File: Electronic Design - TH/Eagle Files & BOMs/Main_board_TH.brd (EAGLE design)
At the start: 90 x 130 mm, 39 parts, among them M1 ARDUINO-NANO-3.0, Q1 IRF9520, Q2 IRF9520

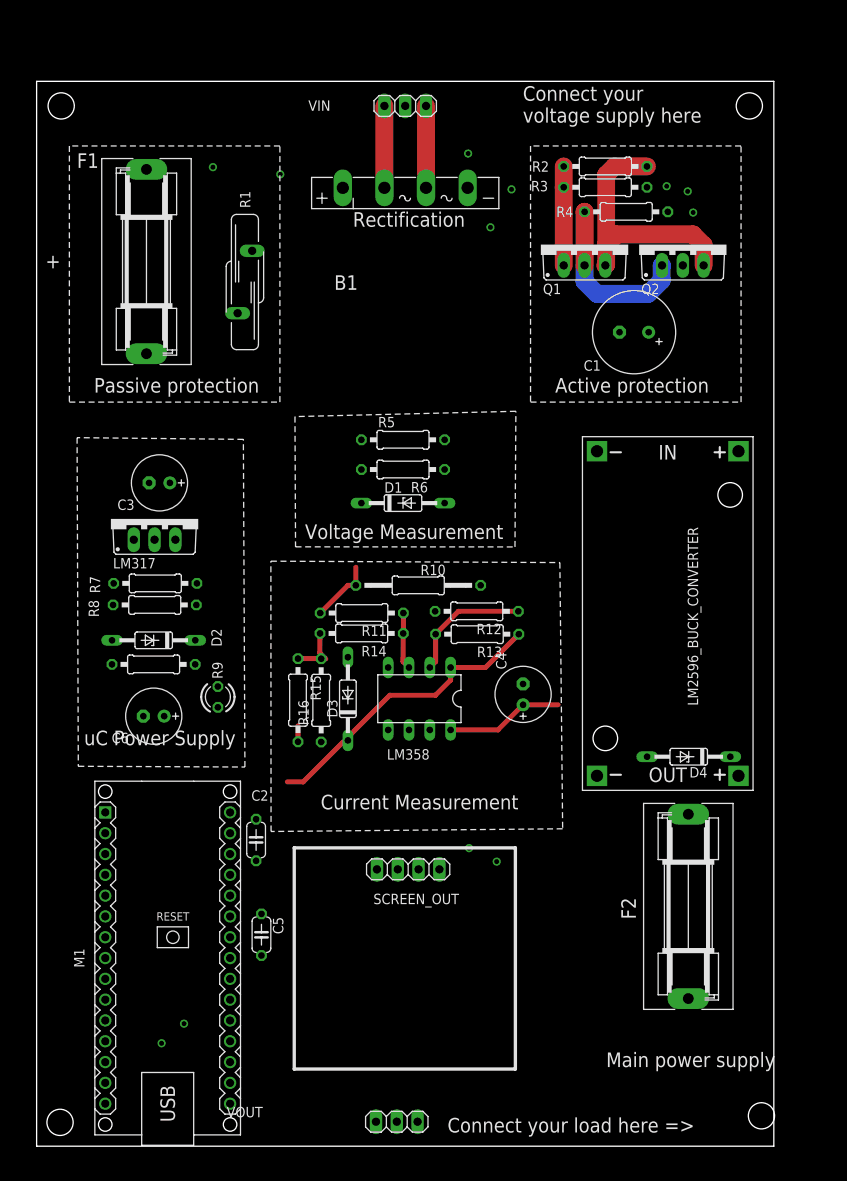
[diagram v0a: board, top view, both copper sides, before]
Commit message: completing power supply alignment and voltage measurement alignment
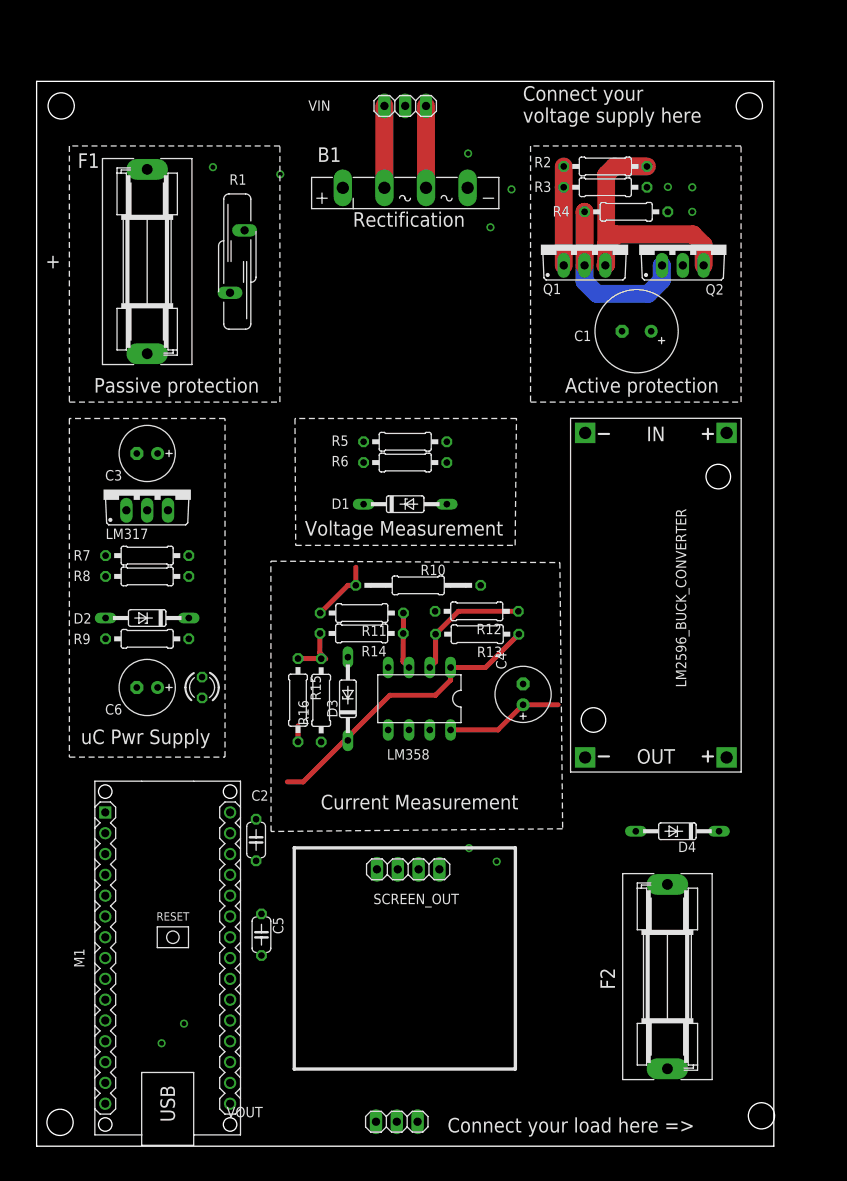
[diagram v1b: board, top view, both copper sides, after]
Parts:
- moved D4 9.20 mm to (78.2, 38.5)
- moved F2 8.94 mm to (77.0, 20.7)
- moved C3 3.89 mm to (13.5, 84.6)
- moved LM317 3.70 mm to (13.5, 80.2)
- moved R8 3.60 mm to (13.5, 69.6)
- moved C6 3.59 mm to (13.5, 56.0)
- moved R7 3.53 mm to (13.5, 72.1)
- moved R9 3.22 mm to (13.5, 61.9)
- moved D2 2.83 mm to (13.5, 64.5)
- moved LM2596_BUCK_CONVERTER 2.67 mm to (75.6, 67.3)
- moved R1 2.67 mm to (24.5, 108.0)
- moved UC_PWR 2.25 mm to (20.2, 56.0), turned to 270 degrees
- moved R6 0.89 mm to (45.0, 83.5)
- moved R5 0.36 mm to (45.0, 86.0)
- moved C1 0.33 mm to (73.2, 99.5)
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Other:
- board text added: "uC Pwr Supply"
- board text removed: "Main power supply"
- board text removed: "uC Power Supply"

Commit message: All placements finished
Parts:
- moved D3 12.7 mm to (45.0, 44.0), turned to 0 degrees
- moved C2 5.12 mm to (27.2, 32.3), turned to 0 degrees
- moved C5 3.93 mm to (27.2, 29.7), turned to 0 degrees
- moved F2 3.58 mm to (75.6, 24.0)
- moved C4 3.40 mm to (56.0, 54.8)
- moved D4 3.05 mm to (75.6, 40.0)
- moved R13 2.44 mm to (51.4, 62.5)
- moved R12 2.40 mm to (51.4, 65.0)
- moved M1 2.33 mm to (14.4, 24.7)
- moved B1 2.00 mm to (45.0, 115.0)
- moved LM358 1.74 mm to (45.0, 54.8)
- moved R15 1.71 mm to (33.6, 54.8)
- moved R10 1.59 mm to (45.0, 68.5)
- moved R16 1.43 mm to (36.1, 54.8)
- moved R11 1.05 mm to (38.6, 65.0)
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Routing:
- net I_IN: track 36.6 -> 0.00 mm
- net N$6: track 15.6 -> 0.00 mm
- net VIN_PROTECTED: track 14.4 -> 0.00 mm
- net N$4: track 7.96 -> 0.00 mm
- net N$5: track 7.25 -> 0.00 mm
- net N$8: track 6.24 -> 0.00 mm
- net N$9: track 10.0 -> 12.0 mm
- net N$7: track 10.0 -> 12.0 mm
- net +5V: track 1.95 -> 0.00 mm
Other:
- board text added: "Output protection"

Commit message: Routing completed
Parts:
- moved D4 28.0 mm to (75.6, 12.0)
- moved UC_PWR 13.1 mm to (8.00, 56.0)
- moved F2 4.00 mm to (75.6, 28.0)
- turned R12 to 0 degrees
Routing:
- net VIN_PROTECTED: track 0.00 -> 176.7 mm
- net +5V: track 0.00 -> 103.4 mm
- net N$10: track 0.00 -> 71.0 mm
- net V_IN: track 0.00 -> 68.9 mm
- net VIN_UNPROTECTED: track 32.0 -> 93.6 mm
- net I_IN: track 0.00 -> 60.3 mm
- net N$4: track 0.00 -> 51.7 mm
- net VOUT_FINAL: track 0.00 -> 48.1 mm
- net A4: track 0.00 -> 44.5 mm
- net A5: track 0.00 -> 31.9 mm
- net N$1: track 0.00 -> 26.1 mm
- net VOUT_PREFUSE: track 0.00 -> 12.0 mm
- net N$23: track 0.00 -> 9.12 mm
- net N$6: track 0.00 -> 6.35 mm
- net N$5: track 0.00 -> 6.35 mm
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- added copper zone on layer 1, net GND
- added copper zone on layer 16, net GND

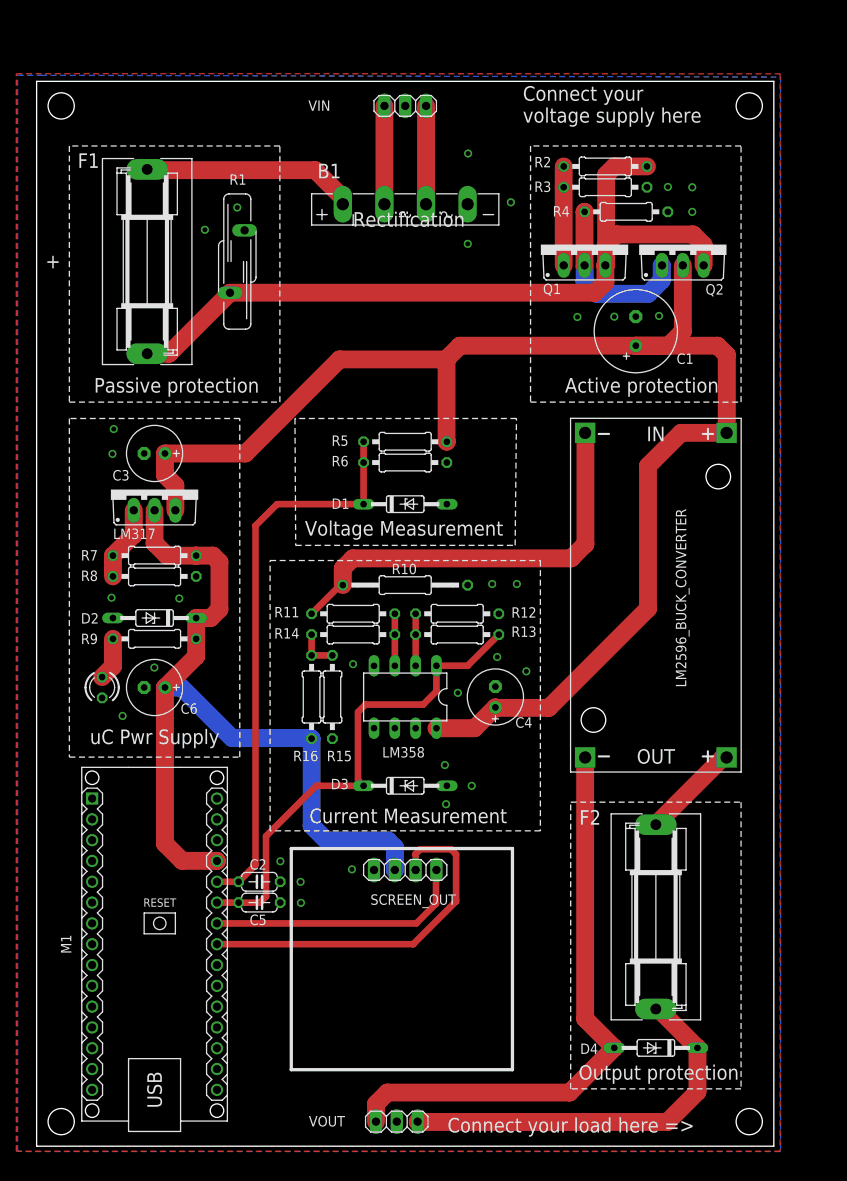
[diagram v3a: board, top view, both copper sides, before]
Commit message: adding in USB outputs
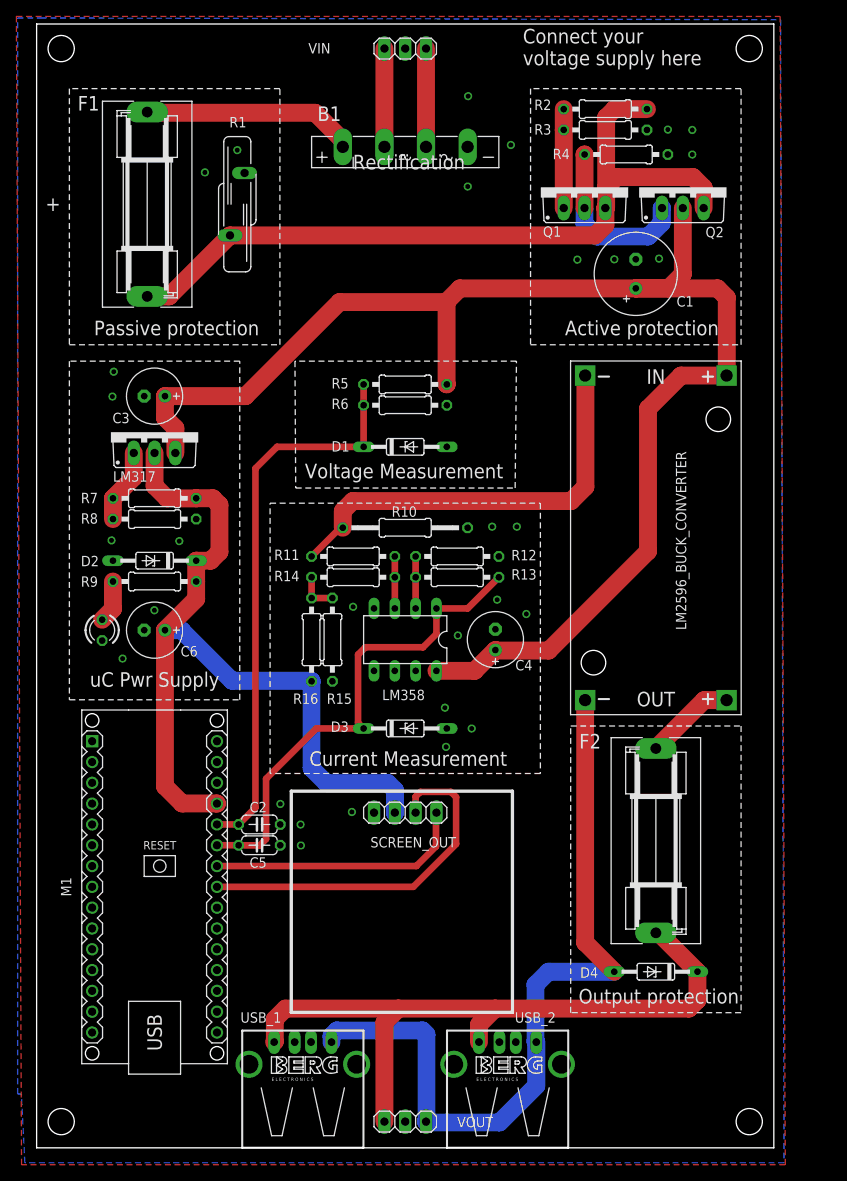
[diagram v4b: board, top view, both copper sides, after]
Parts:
- added USB_1, USB_2: PN87520-S, con-berg:PN87520-S
- moved D4 9.30 mm to (75.6, 21.3)
- moved F2 9.30 mm to (75.6, 37.3)
- moved C5 7.00 mm to (27.2, 36.7)
- moved B1 7.00 mm to (45.0, 122.0)
- moved C1 7.00 mm to (73.2, 106.5)
- moved C2 7.00 mm to (27.2, 39.3)
- moved C3 7.00 mm to (14.4, 91.6)
- moved C4 7.00 mm to (56.0, 61.8)
- moved C6 7.00 mm to (14.4, 63.0)
- moved D1 7.00 mm to (45.0, 85.4)
- moved D2 7.00 mm to (14.4, 71.5)
- moved D3 7.00 mm to (45.0, 51.0)
- moved F1 7.00 mm to (13.5, 115.0)
- moved LM2596_BUCK_CONVERTER 7.00 mm to (75.6, 74.3)
- moved LM317 7.00 mm to (14.4, 87.2)
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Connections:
- net N$10: now also USB_1.4, USB_2.4
- net VOUT_FINAL: now also USB_1.1, USB_2.1
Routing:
- net VOUT_FINAL: track 48.1 -> 85.3 mm
- net N$10: track 71.0 -> 96.1 mm
- net VOUT_PREFUSE: track 12.0 -> 11.1 mm
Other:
- board size 90 x 130 mm -> 90 x 137.2 mm
- board text removed: "Connect your load here =>"

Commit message: Minor cosmetic changes
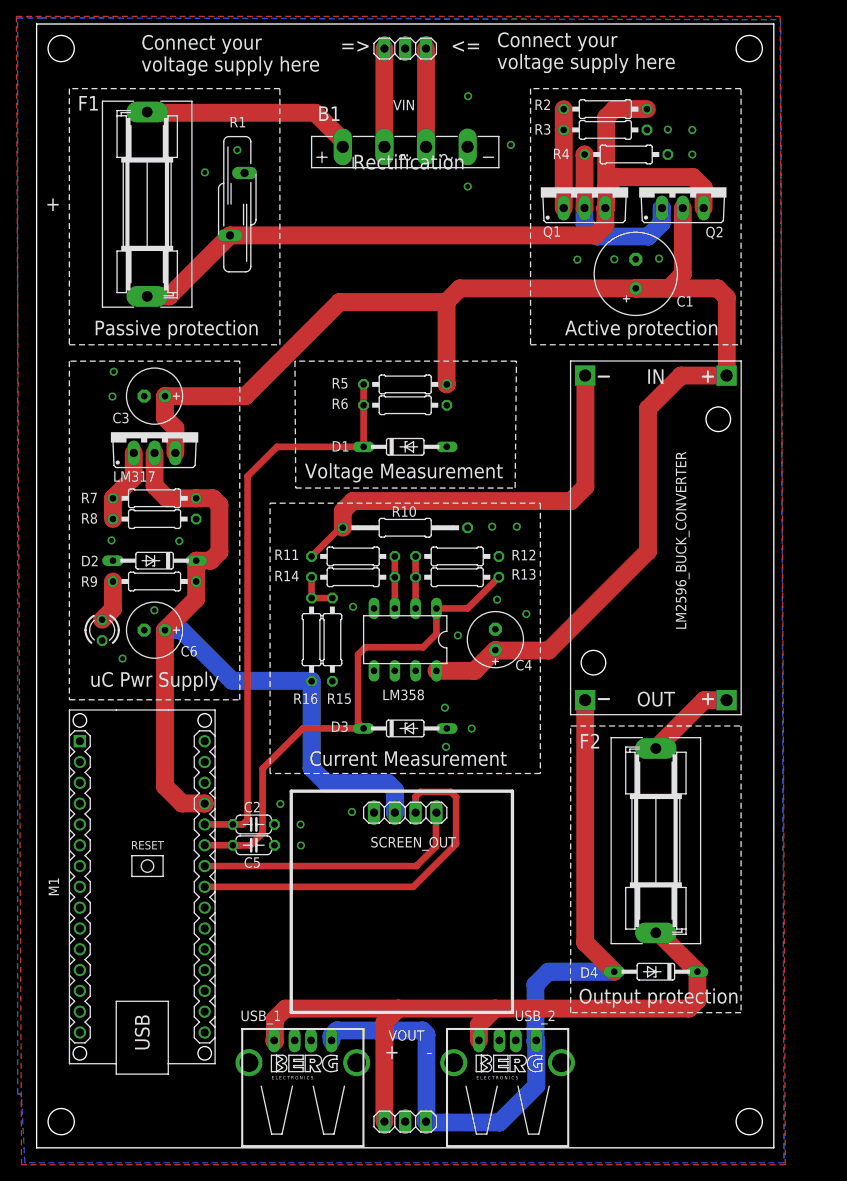
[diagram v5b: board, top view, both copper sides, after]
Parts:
- moved M1 1.50 mm to (12.9, 31.7)
- moved C2 0.70 mm to (26.5, 39.3)
- moved C5 0.70 mm to (26.5, 36.7)
- moved USB_1 0.20 mm to (32.5, 10.2)
- moved USB_2 0.20 mm to (57.5, 10.2)
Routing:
- net I_IN: track 60.3 -> 62.9 mm
- net V_IN: track 68.9 -> 70.7 mm
- net A5: track 31.9 -> 33.4 mm
- net A4: track 44.5 -> 46.0 mm
- net +5V: track 103.4 -> 101.9 mm
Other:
- board text added: "-"
- board text added: "<="

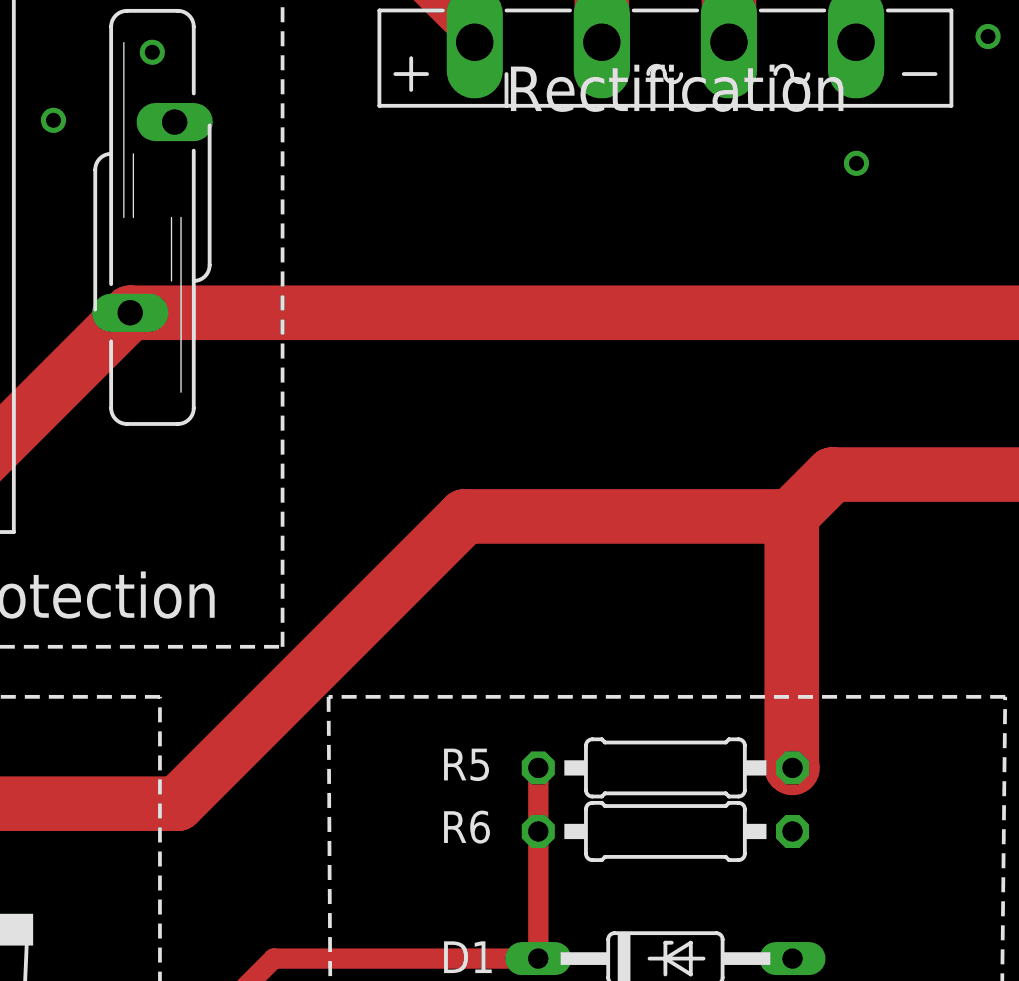
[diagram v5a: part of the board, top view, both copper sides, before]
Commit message: adding logo to the front of the board
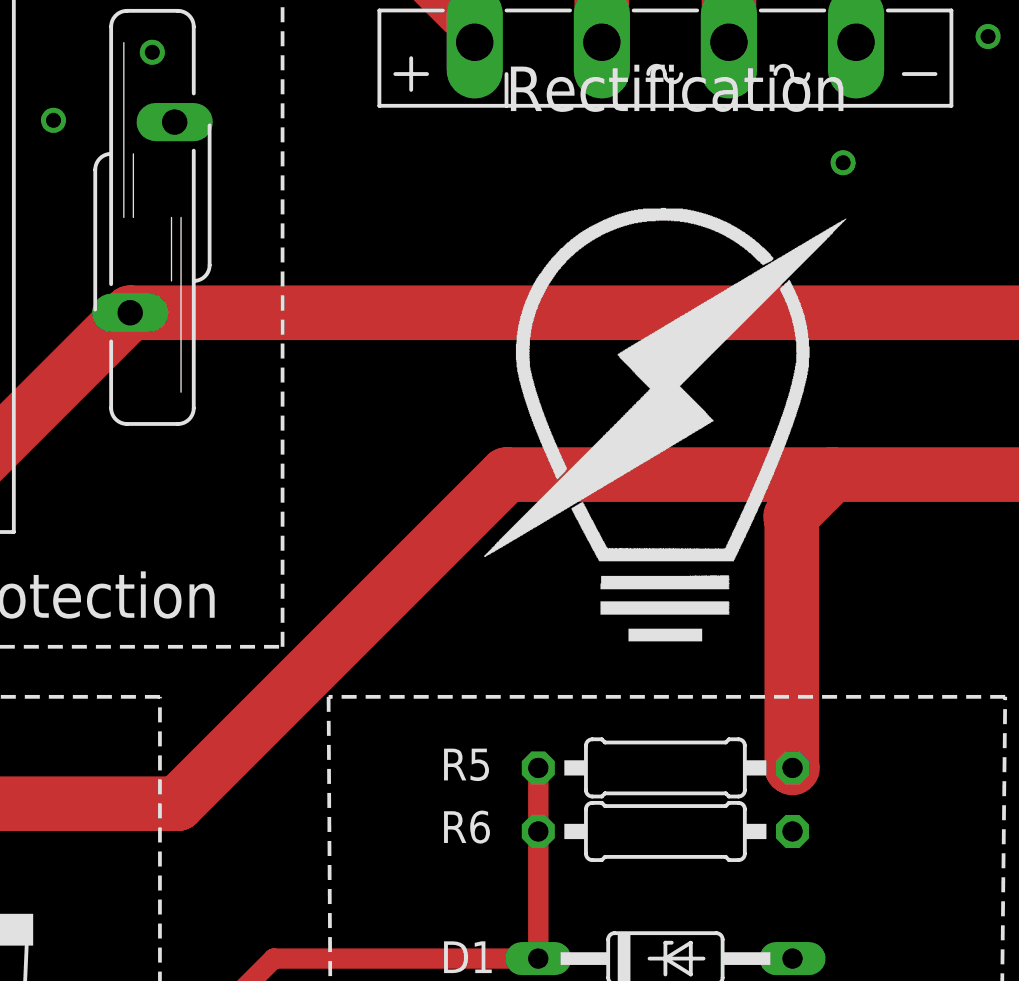
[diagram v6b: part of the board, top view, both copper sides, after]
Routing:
- net VIN_PROTECTED: track 176.7 -> 179.1 mm
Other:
- board text added: "C:/Users/kk/Downloads/path4501.bmp"
